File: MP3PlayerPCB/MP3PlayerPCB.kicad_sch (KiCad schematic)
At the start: 1 part, among them U1 ESP32-WROOM-32

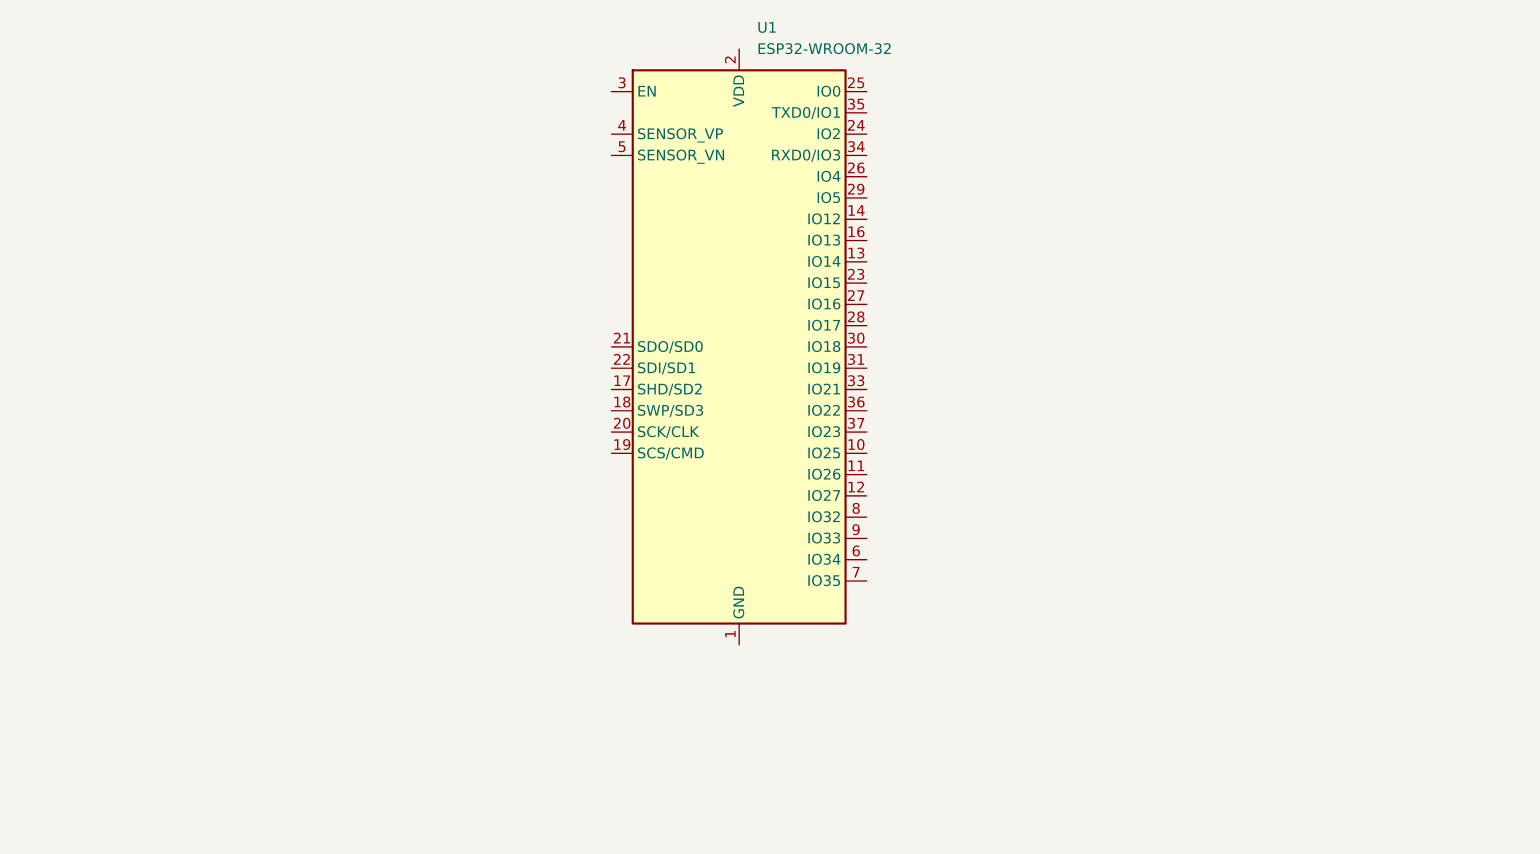
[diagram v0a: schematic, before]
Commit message: - finished schematic for PCB, including all buttons, power management, and connectors.
- May need to add LDO, will confirm after double checking hardware

- Still need to add some footprints
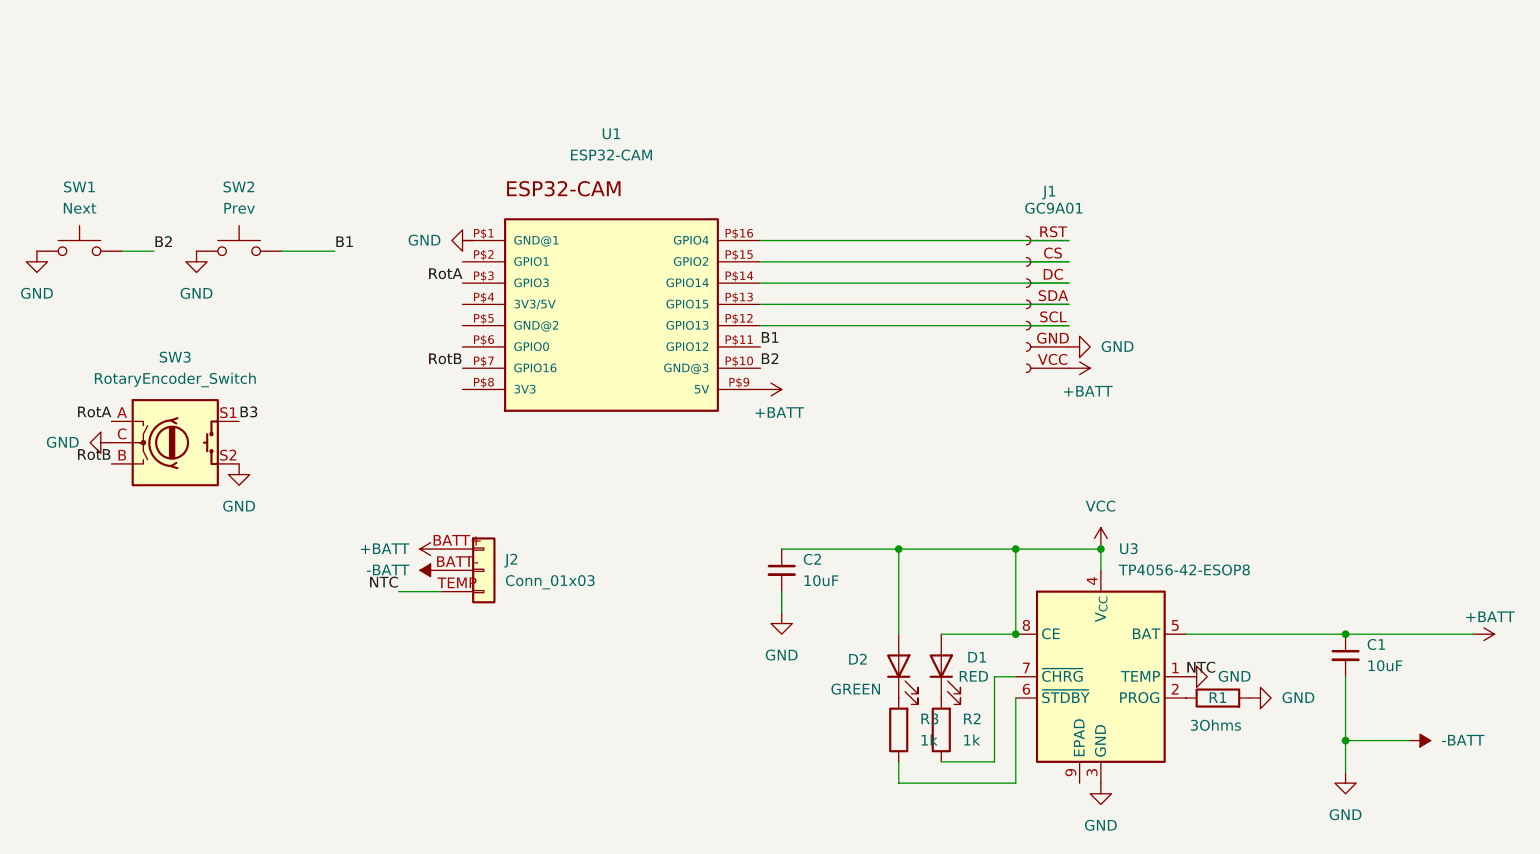
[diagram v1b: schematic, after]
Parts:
- removed U1: ESP32-WROOM-32, RF_Module:ESP32-WROOM-32, symbol RF_Module:ESP32-WROOM-32
- added C1, C2: 10uF, Capacitor_SMD:C_1206_3216Metric_Pad1.33x1.80mm_HandSolder, symbol Device:C_Small
- added D1: RED, LED_SMD:LED_0805_2012Metric_Pad1.15x1.40mm_HandSolder, symbol Device:LED
- added D2: GREEN, LED_SMD:LED_0805_2012Metric_Pad1.15x1.40mm_HandSolder, symbol Device:LED
- added J1: GC9A01, symbol Connector:Conn_01x07_Socket
- added J2: Conn_01x03, symbol Connector_Generic:Conn_01x03
- added R1: 3Ohms, symbol Device:R
- added R2, R3: 1k, symbol Device:R
- added SW1: Next, symbol Switch:SW_Push
- added SW2: Prev, symbol Switch:SW_Push
- added SW3: RotaryEncoder_Switch, symbol Device:RotaryEncoder_Switch
- added U1: ESP32-CAM, ESP32-CAM:ESP32-CAM, symbol ESP32-CAM:ESP32-CAM
- added U3: TP4056-42-ESOP8, Package_SO:SOIC-8-1EP_3.9x4.9mm_P1.27mm_EP2.41x3.3mm_ThermalVias, symbol Battery_Management:TP4056-42-ESOP8
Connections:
- new net: R1.1, U3.2 (PROG)
- new net: R3.1, U3.6 (~{STDBY})
- new net: R2.1, U3.7 (~{CHRG})
- new net: J1.SCL, U1.P$12 (GPIO13)
- new net: J1.SDA, U1.P$13 (GPIO15)
- new net: J1.DC, U1.P$14 (GPIO14)
- new net: J1.CS, U1.P$15 (GPIO2)
- new net: J1.RST, U1.P$16 (GPIO4)
- new net: D2.1 (K), R3.2
- new net: D1.1 (K), R2.2
- new net +BATT: C1.1, J1.VCC, J2.BATT+ (Pin_1), U1.P$9 (5V), U3.5 (BAT)
- new net -BATT: C1.2, C2.2, J1.GND, J2.BATT- (Pin_2), J2.TEMP (Pin_3), R1.2, SW1.1, SW2.1, SW3.C, SW3.S2, U3.1 (TEMP), U3.3 (GND)
- new net B1: SW2.2, U1.P$11 (GPIO12)
- new net B2: SW1.2, U1.P$10 (GND@3)
- new net B3: SW3.S1
- new net RotA: SW3.A, U1.P$3 (GPIO3)
- new net RotB: SW3.B, U1.P$7 (GPIO16)
- new net VCC: C2.1, D1.2 (A), D2.2 (A), U3.4 (V_{CC}), U3.8 (CE)

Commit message: Added all foot prints and routed most of the PCB, will have to do some more hardware verification before PCB if finalized
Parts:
- removed J2: Conn_01x03, symbol Connector_Generic:Conn_01x03
- added J3: Conn_01x02_Socket, Connector_JST:JST_PH_B3B-PH-K_1x03_P2.00mm_Vertical, symbol Connector:Conn_01x02_Socket
- J1: footprint (none) -> GC9A01:GC9A01 TFT
- R1, R2, R3: footprint (none) -> Resistor_SMD:R_0805_2012Metric_Pad1.20x1.40mm_HandSolder
- SW1, SW2: footprint (none) -> Button_Switch_THT:SW_PUSH_6mm
- SW3: footprint (none) -> Rotary_Encoder:RotaryEncoder_Alps_EC11E-Switch_Vertical_H20mm
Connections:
- net +BATT: now also J3.1 (Pin_1)
- net -BATT: now also J3.2 (Pin_2)
